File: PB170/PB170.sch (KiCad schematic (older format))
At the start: 51 parts, among them J2 USB_B_Micro, Q1 P-MOSFET-MLP_HS

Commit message: okay done
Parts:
- removed U?: 74HC08, Housings_SOIC:SOIC-14_3.9x8.7mm_Pitch1.27mm, symbol PB170:74HC08
- removed U? (x4): 74HC74, Package_SO:TSSOP-14_4.4x5mm_P0.65mm, symbol PB170:74HC08
- removed U?: 74HC74, Package_SO:TSSOP-14_4.4x5mm_P0.65mm, symbol Timer:NE555D
- added U?: NE555D, Package_SO:SOIC-8_3.9x4.9mm_P1.27mm, symbol Timer:NE555D
- added U? (x5): 74HC08, Housings_SOIC:SOIC-14_3.9x8.7mm_Pitch1.27mm, symbol PB170:74HC08
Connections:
- net !I0: now also U?.10 (3B), U?.2 (1B)
- net !I1: now also U?.1 (1A), U?.4 (2A)
- net +5V: now also U?.14 (VCC), U?.4 (R), U?.8 (VCC)
- net 00: now also U?.3 (1Y)
- net 01: now also U?.6 (2Y)
- net 10: now also U?.8 (3Y)
- net 11: now also U?.11 (4Y)
- net CLOCK: now also U?.3 (Q)
- net GND: now also U?.1 (GND), U?.7 (GND)
- net I0: now also U?.13 (4B), U?.5 (2B)
- net I1: now also U?.12 (4A), U?.9 (3A)
- net at C?.1, R?.2: now also U?.2 (TR), U?.6 (THR)
- net at C?.1: now also U?.5 (CV)
- net at R?.1, R?.2: now also U?.7 (DIS)
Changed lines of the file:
@@
-$EndComp
-$Comp
-L Timer:NE555D U?
-U 1 1 602EBED7
-P 8450 6400
-F 0 "U?" H 8200 6750 50  0000 C CNN
-F 1 "74HC74" H 8650 6750 50  0000 C CNN
-F 2 "Package_SO:TSSOP-14_4.4x5mm_P0.65mm" H 9300 6000 50  0001 C CNN
-F 3 "https://datasheet.lcsc.com/szlcsc/Texas-Instruments-TI-SN74HC74PWR_C6761.pdf" H 9300 6000 50  0001 C CNN
-F 4 "C7593" H 8450 6400 50  0001 C CNN "LCSC"
-	1    8450 6400
-	1    0    0    -1
 $EndComp
 $Comp
@@
 U 2 1 602C6C00
 P 15000 7050
-F 0 "U?" H 15000 7531 50  0001 C CNN
-F 1 "74HC74" H 15000 7440 50  0001 C CNN
+F 0 "U?" H 15000 7531 50  0000 C CNN
+F 1 "74HC74" H 15000 7440 50  0000 C CNN
 F 2 "Package_SO:TSSOP-14_4.4x5mm_P0.65mm" H 15000 7050 50  0001 C CNN
 F 3 "https://datasheet.lcsc.com/szlcsc/Texas-Instruments-TI-SN74HC74PWR_C6761.pdf" H 15000 7050 50  0001 C CNN
@@
 $EndSheet
 $Comp
-L PB170:74HC08 U?
-U 1 1 60263149
-P 11800 8200
-F 0 "U?" H 11825 8467 50  0000 C CNN
-F 1 "74HC08" H 11825 8376 50  0000 C CNN
-F 2 "Housings_SOIC:SOIC-14_3.9x8.7mm_Pitch1.27mm" H 11800 8200 50  0001 C CNN
-F 3 "https://datasheet.lcsc.com/szlcsc/Nexperia-74HC08D-653_C5593.pdf" H 11800 8200 50  0001 C CNN
-F 4 "C5593" H 11800 8200 50  0001 C CNN "LCSC"
-	1    11800 8200
-	1    0    0    -1
-$EndComp
-$Comp
-L PB170:74HC08 U?
-U 2 1 6026408A
-P 11800 8700
-F 0 "U?" H 11825 8967 50  0000 C CNN
-F 1 "74HC74" H 11825 8876 50  0000 C CNN
-F 2 "Package_SO:TSSOP-14_4.4x5mm_P0.65mm" H 11800 8700 50  0001 C CNN
-F 3 "https://datasheet.lcsc.com/szlcsc/Texas-Instruments-TI-SN74HC74PWR_C6761.pdf" H 11800 8700 50  0001 C CNN
-F 4 "C5593" H 11800 8700 50  0001 C CNN "LCSC"
-	2    11800 8700
-	1    0    0    -1
-$EndComp
-$Comp
-L PB170:74HC08 U?
-U 3 1 60264C31
-P 11800 9200
-F 0 "U?" H 11825 9467 50  0000 C CNN
-F 1 "74HC74" H 11825 9376 50  0000 C CNN
-F 2 "Package_SO:TSSOP-14_4.4x5mm_P0.65mm" H 11800 9200 50  0001 C CNN
-F 3 "https://datasheet.lcsc.com/szlcsc/Texas-Instruments-TI-SN74HC74PWR_C6761.pdf" H 11800 9200 50  0001 C CNN
-F 4 "C5593" H 11800 9200 50  0001 C CNN "LCSC"
-	3    11800 9200
-	1    0    0    -1
-$EndComp
-$Comp
-L PB170:74HC08 U?
-U 4 1 602660AC
-P 11800 9700
-F 0 "U?" H 11825 9967 50  0000 C CNN
-F 1 "74HC74" H 11825 9876 50  0000 C CNN
-F 2 "Package_SO:TSSOP-14_4.4x5mm_P0.65mm" H 11800 9700 50  0001 C CNN
-F 3 "https://datasheet.lcsc.com/szlcsc/Texas-Instruments-TI-SN74HC74PWR_C6761.pdf" H 11800 9700 50  0001 C CNN
-F 4 "C5593" H 11800 9700 50  0001 C CNN "LCSC"
-	4    11800 9700
-	1    0    0    -1
-$EndComp
-$Comp
-L PB170:74HC08 U?
-U 5 1 60266D07
-P 12850 8950
-F 0 "U?" H 13080 8996 50  0000 L CNN
-F 1 "74HC74" H 13080 8905 50  0000 L CNN
-F 2 "Package_SO:TSSOP-14_4.4x5mm_P0.65mm" H 12850 8950 50  0001 C CNN
-F 3 "https://datasheet.lcsc.com/szlcsc/Texas-Instruments-TI-SN74HC74PWR_C6761.pdf" H 12850 8950 50  0001 C CNN
-F 4 "C5593" H 12850 8950 50  0001 C CNN "LCSC"
-	5    12850 8950
-	1    0    0    -1
-$EndComp
-$Comp
 L 74xx:74HC74 U?
 U 2 1 60267249
@@
 Wire Wire Line
 	15500 7550 15500 7700
+$Comp
+L PB170:74HC08 U?
+U 1 1 60281F71
+P 11800 8200
+F 0 "U?" H 11825 8467 50  0000 C CNN
+F 1 "74HC08" H 11825 8376 50  0000 C CNN
+F 2 "Housings_SOIC:SOIC-14_3.9x8.7mm_Pitch1.27mm" H 11800 8200 50  0001 C CNN
+F 3 "https://datasheet.lcsc.com/szlcsc/Nexperia-74HC08D-653_C5593.pdf" H 11800 8200 50  0001 C CNN
+F 4 "C5593" H 11800 8200 50  0001 C CNN "LCSC"
+	1    11800 8200
+	1    0    0    -1
+$EndComp
+$Comp
+L PB170:74HC08 U?
+U 2 1 602838AE
+P 11800 8700
+F 0 "U?" H 11825 8967 50  0000 C CNN
+F 1 "74HC08" H 11825 8876 50  0000 C CNN
+F 2 "Housings_SOIC:SOIC-14_3.9x8.7mm_Pitch1.27mm" H 11800 8700 50  0001 C CNN
+F 3 "https://datasheet.lcsc.com/szlcsc/Nexperia-74HC08D-653_C5593.pdf" H 11800 8700 50  0001 C CNN
+F 4 "C5593" H 11800 8700 50  0001 C CNN "LCSC"
+	2    11800 8700
+	1    0    0    -1
+$EndComp
+$Comp
+L PB170:74HC08 U?
+U 3 1 60284736
+P 11800 9200
+F 0 "U?" H 11825 9467 50  0000 C CNN
+F 1 "74HC08" H 11825 9376 50  0000 C CNN
+F 2 "Housings_SOIC:SOIC-14_3.9x8.7mm_Pitch1.27mm" H 11800 9200 50  0001 C CNN
+F 3 "https://datasheet.lcsc.com/szlcsc/Nexperia-74HC08D-653_C5593.pdf" H 11800 9200 50  0001 C CNN
+F 4 "C5593" H 11800 9200 50  0001 C CNN "LCSC"
+	3    11800 9200
+	1    0    0    -1
+$EndComp
+$Comp
+L PB170:74HC08 U?
+U 4 1 60285211
+P 11800 9700
+F 0 "U?" H 11825 9967 50  0000 C CNN
+F 1 "74HC08" H 11825 9876 50  0000 C CNN
+F 2 "Housings_SOIC:SOIC-14_3.9x8.7mm_Pitch1.27mm" H 11800 9700 50  0001 C CNN
+F 3 "https://datasheet.lcsc.com/szlcsc/Nexperia-74HC08D-653_C5593.pdf" H 11800 9700 50  0001 C CNN
+F 4 "C5593" H 11800 9700 50  0001 C CNN "LCSC"
+	4    11800 9700
+	1    0    0    -1
+$EndComp
+$Comp
+L PB170:74HC08 U?
+U 5 1 60285E84
+P 12850 8950
+F 0 "U?" H 13080 8996 50  0000 L CNN
+F 1 "74HC08" H 13080 8905 50  0000 L CNN
+F 2 "Housings_SOIC:SOIC-14_3.9x8.7mm_Pitch1.27mm" H 12850 8950 50  0001 C CNN
+F 3 "https://datasheet.lcsc.com/szlcsc/Nexperia-74HC08D-653_C5593.pdf" H 12850 8950 50  0001 C CNN
+F 4 "C5593" H 12850 8950 50  0001 C CNN "LCSC"
+	5    12850 8950
+	1    0    0    -1
+$EndComp
+$Comp
+L Timer:NE555D U?
+U 1 1 60274CEE
+P 8450 6400
+F 0 "U?" H 8450 6981 50  0000 C CNN
+F 1 "NE555D" H 8450 6890 50  0000 C CNN
+F 2 "Package_SO:SOIC-8_3.9x4.9mm_P1.27mm" H 9300 6000 50  0001 C CNN
+F 3 "https://datasheet.lcsc.com/szlcsc/Texas-Instruments-TI-NE555DR_C7593.pdf" H 9300 6000 50  0001 C CNN
+F 4 " C7593" H 8450 6400 50  0001 C CNN "LCSc"
+	1    8450 6400
+	1    0    0    -1
+$EndComp
 $EndSCHEMATC

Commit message: refs changed
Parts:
- removed U?: NE555D, Package_SO:SOIC-8_3.9x4.9mm_P1.27mm, symbol Timer:NE555D
- removed U? (x5): 74HC08, Housings_SOIC:SOIC-14_3.9x8.7mm_Pitch1.27mm, symbol PB170:74HC08
- added U1: 74HC00, Package_SO:TSSOP-14_4.4x5mm_P0.65mm, symbol 74xx:74HC00
- added U2, U3, U4, U5, U6: 74HC08, Housings_SOIC:SOIC-14_3.9x8.7mm_Pitch1.27mm, symbol PB170:74HC08
- added U7, U8, U9: 74HC32, Housings_SOIC:SOIC-14_3.9x8.7mm_Pitch1.27mm, symbol PB170:74HC32
- added U?: NE555D, Package_SO:SOIC-8_3.9x4.9mm_P1.27mm, symbol Timer:NE555D
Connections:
- net !I0: now also U3.13 (4B), U5.13 (4B), U6.10 (3B), U6.2 (1B)
- net !I1: now also U6.1 (1A), U6.4 (2A)
- net +5V: now also U1.14 (VCC), U2.14 (VCC), U3.14 (VCC), U4.14 (VCC), U5.14 (VCC), U6.14 (VCC), U7.14 (VCC), U8.14 (VCC), U9.14 (VCC), U?.4 (R), U?.8 (VCC)
- net 00: now also U1.10, U1.9, U6.3 (1Y)
- net 01: now also U1.4, U1.5, U3.2 (1B), U5.5 (2B), U6.6 (2Y)
- net 10: now also U1.12, U1.13, U2.10 (3B), U4.2 (1B), U5.2 (1B), U6.8 (3Y)
- net 11: now also U1.1, U1.2, U2.5 (2B), U3.10 (3B), U3.5 (2B), U5.10 (3B), U6.11 (4Y)
- net CLOCK: now also U?.3 (Q)
- net GND: now also U1.7 (GND), U2.7 (GND), U3.7 (GND), U4.7 (GND), U5.7 (GND), U6.7 (GND), U7.7 (GND), U8.7 (GND), U9.7 (GND), U?.1 (GND)
- net I0: now also U6.13 (4B), U6.5 (2B)
- net I1: now also U4.10 (3B), U6.12 (4A), U6.9 (3A)
- net LA: now also U7.8 (3Y)
- net LB: now also U8.3 (1Y)
- net LC: now also U8.11 (4Y)
- net LD: now also U9.3 (1Y)
- net LE: now also U9.11 (4Y)
- net Q0: now also U2.1 (1A), U3.9 (3A), U4.9 (3A), U5.1 (1A)
- net Q1: now also U2.12 (4A), U5.4 (2A)
- net Q2: now also U2.4 (2A), U3.1 (1A), U3.12 (4A), U5.9 (3A)
- net Q3: now also U3.4 (2A), U4.1 (1A), U4.12 (4A), U7.1 (1A)
- net Q4: now also U4.4 (2A), U5.12 (4A), U7.2 (1B)
- net at C?.1, R?.2: now also U?.2 (TR), U?.6 (THR)
- net at C?.1: now also U?.5 (CV)
- net at R?.1, R?.2: now also U?.7 (DIS)
- new net: U2.9 (3A), U7.3 (1Y)
- new net: U1.3, U2.2 (1B)
- new net: U2.3 (1Y), U7.4 (2A)
- new net: U2.6 (2Y), U7.5 (2B)
- new net: U7.6 (2Y), U7.9 (3A)
- new net: U3.8 (3Y), U8.4 (2A)
- new net: U3.11 (4Y), U8.5 (2B)
- new net: U8.12 (4A), U8.6 (2Y)
- new net: U4.6 (2Y), U8.10 (3B)
- new net: U8.13 (4B), U8.8 (3Y)
- new net: U4.3 (1Y), U8.9 (3A)
- new net: U4.8 (3Y), U9.1 (1A)
- new net: U4.11 (4Y), U9.2 (1B)
- new net: U5.11 (4Y), U9.10 (3B)
- new net: U9.13 (4B), U9.8 (3Y)
- new net: U5.8 (3Y), U9.9 (3A)
- new net: U2.8 (3Y), U7.10 (3B)
- new net: U7.11 (4Y), U8.1 (1A)
- new net: U2.11 (4Y), U7.12 (4A)
- new net: U3.3 (1Y), U7.13 (4B)
- new net: U3.6 (2Y), U8.2 (1B)
- new net: U1.6, U2.13 (4B)
- new net: U1.8, U4.5 (2B)
- new net: U1.11, U4.13 (4B)
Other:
- moved on the sheet: C?, D?, H1, H2, H3, H4, J2, R11, R?, SW?, U?A, U?B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

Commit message: annotated, needs footprints exported
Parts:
- U14: renamed from U?; value NE555D -> 74HC74; footprint Package_SO:SOIC-8_3.9x4.9mm_P1.27mm -> Package_SO:TSSOP-14_4.4x5mm_P0.65mm
- gave numbers to parts that had none: 24

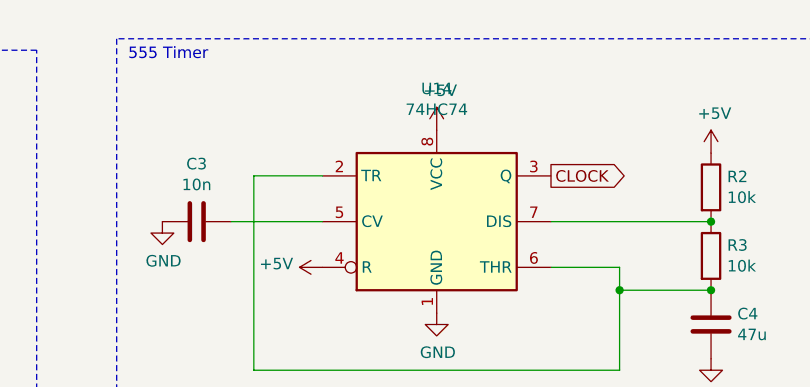
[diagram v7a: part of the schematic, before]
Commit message: need needs capacitor footprints
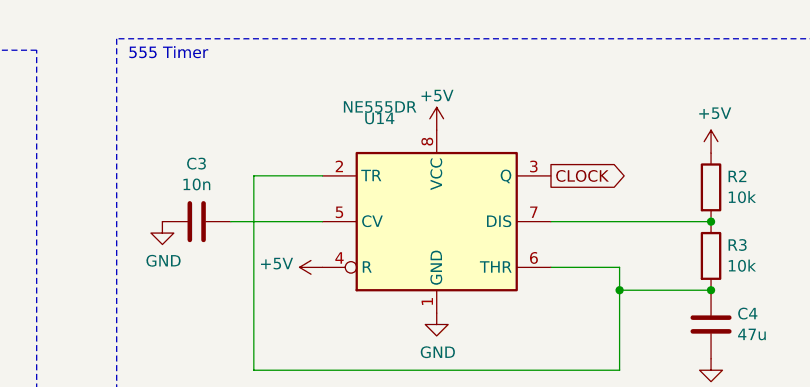
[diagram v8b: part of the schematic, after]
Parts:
- C1: footprint Capacitors_SMD:C_0805 -> PB170:C0805
- D1, D2, D3, D4, D5, D6: footprint LEDs:LED_0603 -> PB170:LED0603-R-RD
- R1, R10, R11, R12, R4, R5, R6, R7, R8, R9: footprint Resistors_SMD:R_0603 -> PB170:R0603
- R2, R3: footprint Resistor_SMD:R_0402_1005Metric -> PB170:R0603; LCSC (none) -> C25804
- U1, U10, U11, U12, U13: footprint Package_SO:TSSOP-14_4.4x5mm_P0.65mm -> PB170:TSSOP-14_L5.0-W4.4-P0.65-LS6.4-BL
- U14: value 74HC74 -> NE555DR; footprint Package_SO:TSSOP-14_4.4x5mm_P0.65mm -> PB170:SOIC-8_L4.9-W3.9-P1.27-LS6.0-BL; LCSC (none) -> C7593
- U2, U3, U4, U5, U7, U8, U9: footprint Housings_SOIC:SOIC-14_3.9x8.7mm_Pitch1.27mm -> PB170:SOIC-14_L8.7-W3.9-P1.27-LS6.0-BL
